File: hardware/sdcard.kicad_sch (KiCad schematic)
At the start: 15 parts, among them J1 MEM2067

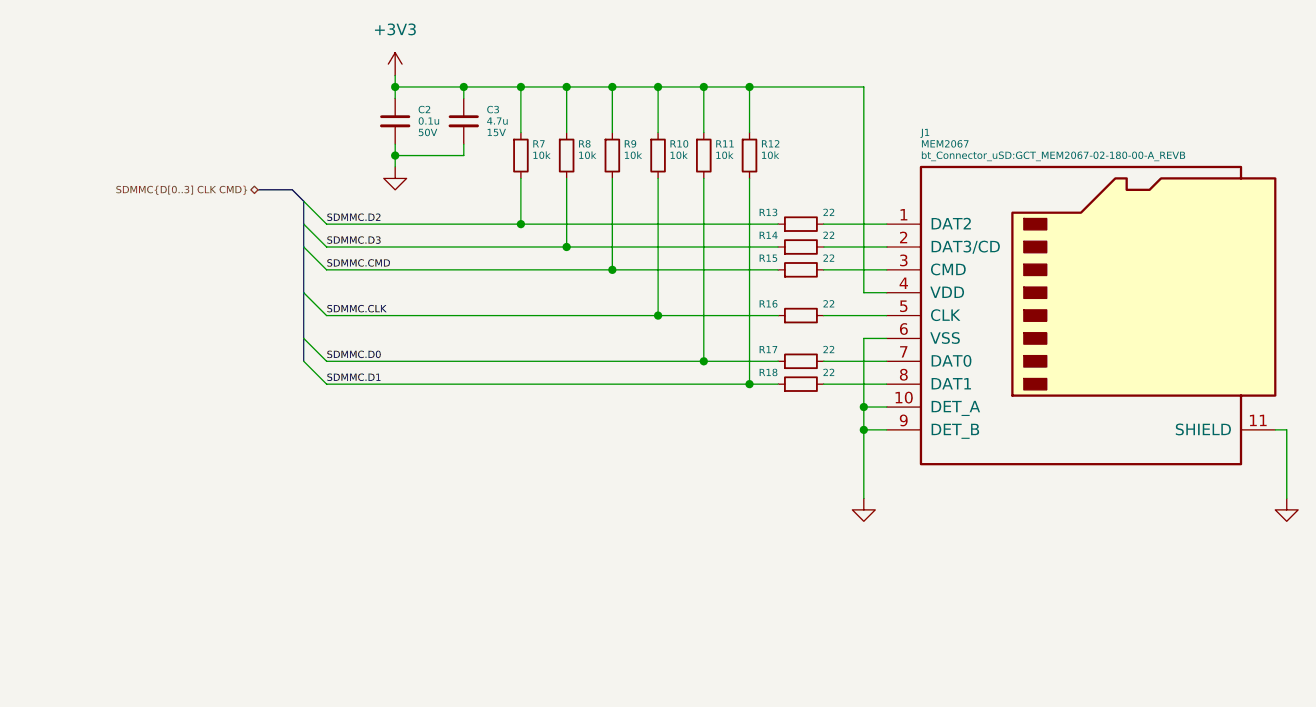
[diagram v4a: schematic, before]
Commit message: merged in lcdboard test work
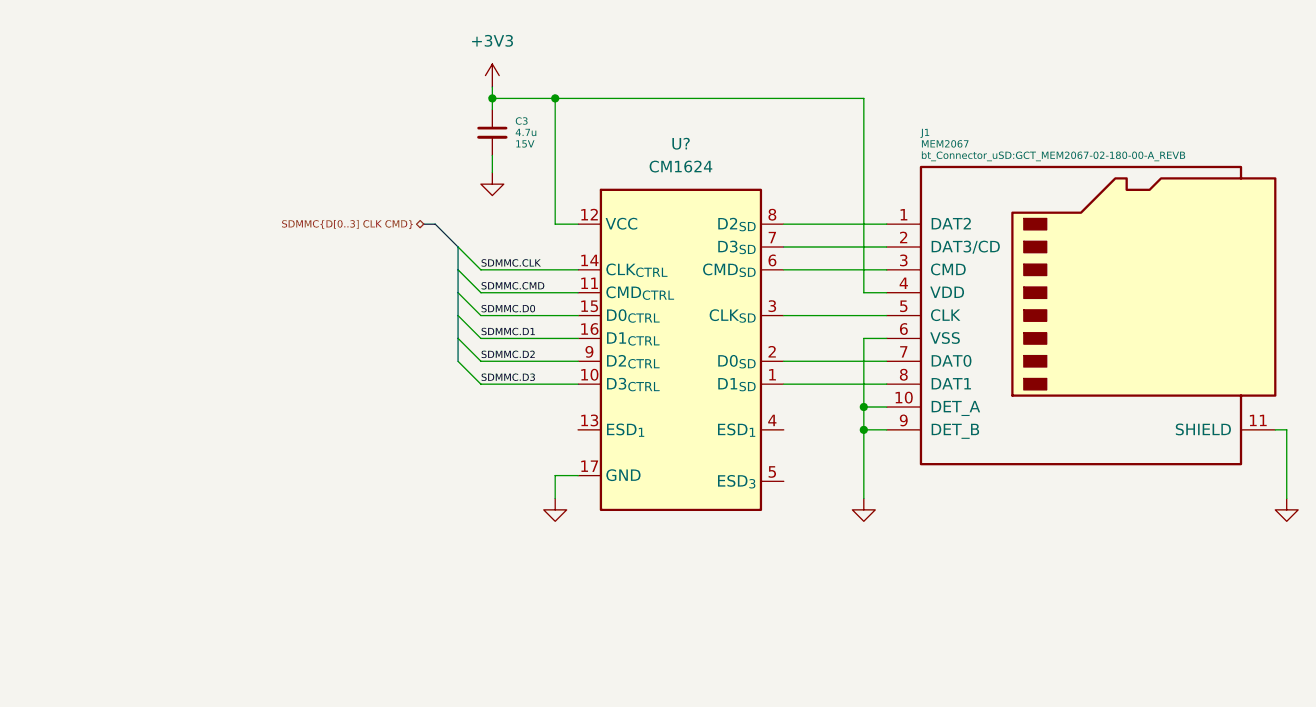
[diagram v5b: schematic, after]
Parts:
- removed C2: 0.1u, Capacitor_SMD:C_0402_1005Metric, symbol Device:C_Small
- removed R10, R11, R12, R7, R8, R9: 10k, Resistor_SMD:R_0402_1005Metric, symbol Device:R_Small
- removed R13, R14, R15, R16, R17, R18: 22, Resistor_SMD:R_0402_1005Metric, symbol Device:R_Small
- added U?: CM1624, symbol bt_Protection:CM1624
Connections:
- net +3V3: now also U?.12 (VCC)
- net GND: now also U?.17 (GND)
- net SDMMC.CLK: now also U?.14 (CLK_{CTRL})
- net SDMMC.CMD: now also U?.11 (CMD_{CTRL})
- net SDMMC.D0: now also U?.15 (D0_{CTRL})
- net SDMMC.D1: now also U?.16 (D1_{CTRL})
- net SDMMC.D2: now also U?.9 (D2_{CTRL})
- net SDMMC.D3: now also U?.10 (D3_{CTRL})
- net at J1.8 (DAT1): now also U?.1 (D1_{SD})
- net at J1.2 (DAT3/CD): now also U?.7 (D3_{SD})
- net at J1.7 (DAT0): now also U?.2 (D0_{SD})
- net at J1.5 (CLK): now also U?.3 (CLK_{SD})
- net at J1.1 (DAT2): now also U?.8 (D2_{SD})
- net at J1.3 (CMD): now also U?.6 (CMD_{SD})
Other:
- moved on the sheet: C3
